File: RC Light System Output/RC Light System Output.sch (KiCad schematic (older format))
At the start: 4 parts, among them J1 INPUT, J2 CHAIN, U1 74HC595

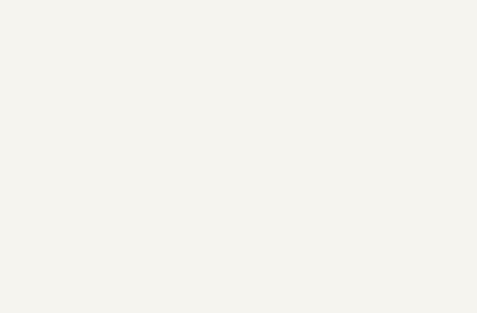
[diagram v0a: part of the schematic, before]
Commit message: Map footprints and add transistor pulldowns
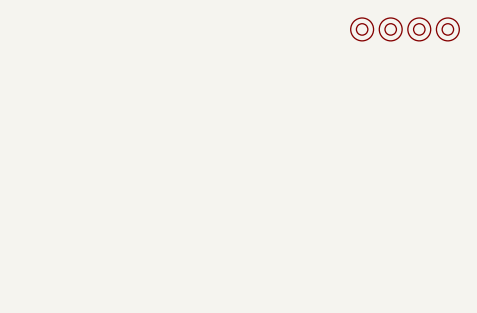
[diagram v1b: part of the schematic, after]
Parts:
- added M1, M2, M3, M4: Mounting, mounting:M3, symbol mounting:Mounting
- C1: footprint (none) -> Capacitor_THT:C_Disc_D4.7mm_W2.5mm_P5.00mm
- J1, J2: footprint (none) -> Connector_JST:JST_XH_B6B-XH-A_1x06_P2.50mm_Vertical
- U1: footprint (none) -> Package_DIP:DIP-16_W7.62mm_Socket_LongPads
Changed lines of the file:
@@
 F 0 "U1" H 6225 4000 50  0000 L CNN
 F 1 "74HC595" H 6225 3925 50  0000 L CNN
-F 2 "" H 6175 3350 50  0001 C CNN
+F 2 "Package_DIP:DIP-16_W7.62mm_Socket_LongPads" H 6175 3350 50  0001 C CNN
 F 3 "http://www.ti.com/lit/ds/symlink/sn74hc595.pdf" H 6175 3350 50  0001 C CNN
 	1    6175 3350
@@
 F 0 "C1" H 6592 7196 50  0000 L CNN
 F 1 "100nF" H 6592 7105 50  0000 L CNN
-F 2 "" H 6500 7150 50  0001 C CNN
+F 2 "Capacitor_THT:C_Disc_D4.7mm_W2.5mm_P5.00mm" H 6500 7150 50  0001 C CNN
 F 3 "~" H 6500 7150 50  0001 C CNN
 	1    6500 7150
@@
 F 0 "J1" H 4025 3450 50  0000 C CNN
 F 1 "INPUT" H 4025 3375 50  0000 C CNN
-F 2 "" H 3925 3075 50  0001 C CNN
+F 2 "Connector_JST:JST_XH_B6B-XH-A_1x06_P2.50mm_Vertical" H 3925 3075 50  0001 C CNN
 F 3 "~" H 3925 3075 50  0001 C CNN
 	1    3925 3075
@@
 F 0 "J2" H 4025 4900 50  0000 C CNN
 F 1 "CHAIN" H 4025 4825 50  0000 C CNN
-F 2 "" H 3925 4525 50  0001 C CNN
+F 2 "Connector_JST:JST_XH_B6B-XH-A_1x06_P2.50mm_Vertical" H 3925 4525 50  0001 C CNN
 F 3 "~" H 3925 4525 50  0001 C CNN
 	1    3925 4525
@@
 Wire Wire Line
 	6575 3650 7400 3650
+$Comp
+L mounting:Mounting M1
+U 1 1 6509087E
+P 10575 550
+F 0 "M1" H 10575 650 50  0001 C CNN
+F 1 "Mounting" H 10575 475 50  0001 C CNN
+F 2 "mounting:M3" H 10575 550 50  0001 C CNN
+F 3 "~" H 10575 550 50  0001 C CNN
+	1    10575 550
+	1    0    0    -1
+$EndComp
+$Comp
+L mounting:Mounting M2
+U 1 1 65090F96
+P 10700 550
+F 0 "M2" H 10700 650 50  0001 C CNN
+F 1 "Mounting" H 10700 475 50  0001 C CNN
+F 2 "mounting:M3" H 10700 550 50  0001 C CNN
+F 3 "~" H 10700 550 50  0001 C CNN
+	1    10700 550
+	1    0    0    -1
+$EndComp
+$Comp
+L mounting:Mounting M3
+U 1 1 65091332
+P 10825 550
+F 0 "M3" H 10825 650 50  0001 C CNN
+F 1 "Mounting" H 10825 475 50  0001 C CNN
+F 2 "mounting:M3" H 10825 550 50  0001 C CNN
+F 3 "~" H 10825 550 50  0001 C CNN
+	1    10825 550
+	1    0    0    -1
+$EndComp
+$Comp
+L mounting:Mounting M4
+U 1 1 65091634
+P 10950 550
+F 0 "M4" H 10950 650 50  0001 C CNN
+F 1 "Mounting" H 10950 475 50  0001 C CNN
+F 2 "mounting:M3" H 10950 550 50  0001 C CNN
+F 3 "~" H 10950 550 50  0001 C CNN
+	1    10950 550
+	1    0    0    -1
+$EndComp
 $EndSCHEMATC

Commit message: Big boy output layout
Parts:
- removed M1, M2, M3, M4: Mounting, mounting:M3, symbol mounting:Mounting
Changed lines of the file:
@@
 Wire Wire Line
 	6575 3650 7400 3650
-$Comp
-L mounting:Mounting M1
-U 1 1 6509087E
-P 10575 550
-F 0 "M1" H 10575 650 50  0001 C CNN
-F 1 "Mounting" H 10575 475 50  0001 C CNN
-F 2 "mounting:M3" H 10575 550 50  0001 C CNN
-F 3 "~" H 10575 550 50  0001 C CNN
-	1    10575 550
-	1    0    0    -1
-$EndComp
-$Comp
-L mounting:Mounting M2
-U 1 1 65090F96
-P 10700 550
-F 0 "M2" H 10700 650 50  0001 C CNN
-F 1 "Mounting" H 10700 475 50  0001 C CNN
-F 2 "mounting:M3" H 10700 550 50  0001 C CNN
-F 3 "~" H 10700 550 50  0001 C CNN
-	1    10700 550
-	1    0    0    -1
-$EndComp
-$Comp
-L mounting:Mounting M3
-U 1 1 65091332
-P 10825 550
-F 0 "M3" H 10825 650 50  0001 C CNN
-F 1 "Mounting" H 10825 475 50  0001 C CNN
-F 2 "mounting:M3" H 10825 550 50  0001 C CNN
-F 3 "~" H 10825 550 50  0001 C CNN
-	1    10825 550
-	1    0    0    -1
-$EndComp
-$Comp
-L mounting:Mounting M4
-U 1 1 65091634
-P 10950 550
-F 0 "M4" H 10950 650 50  0001 C CNN
-F 1 "Mounting" H 10950 475 50  0001 C CNN
-F 2 "mounting:M3" H 10950 550 50  0001 C CNN
-F 3 "~" H 10950 550 50  0001 C CNN
-	1    10950 550
-	1    0    0    -1
-$EndComp
 $EndSCHEMATC
